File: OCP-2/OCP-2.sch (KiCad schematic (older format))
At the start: 176 parts, among them X1 ico*отверстие*М3, X2 ico*отверстие*М3, X3 ico*отверстие*М3, X4 ico*отверстие*М3

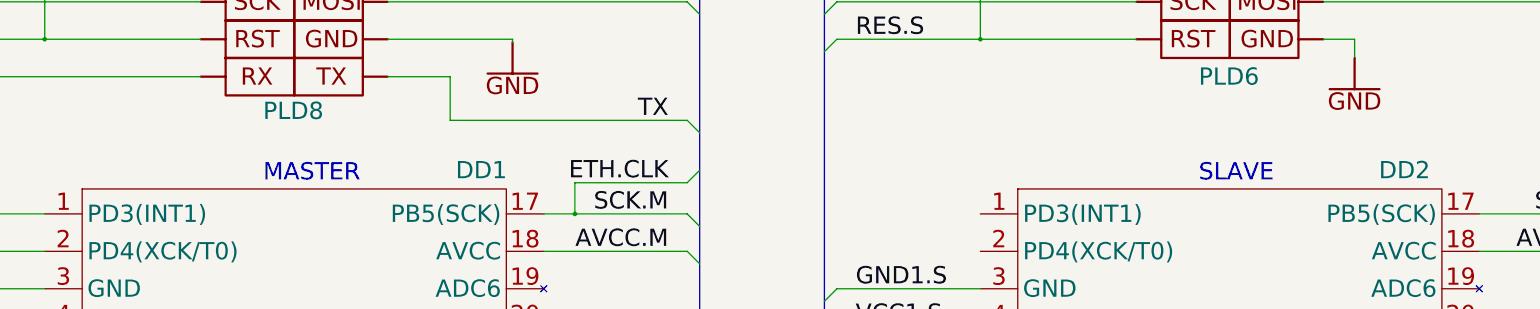
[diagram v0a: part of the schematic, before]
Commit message: перенесены клеммники, +LDO, +прог.разъем, +МК расположение
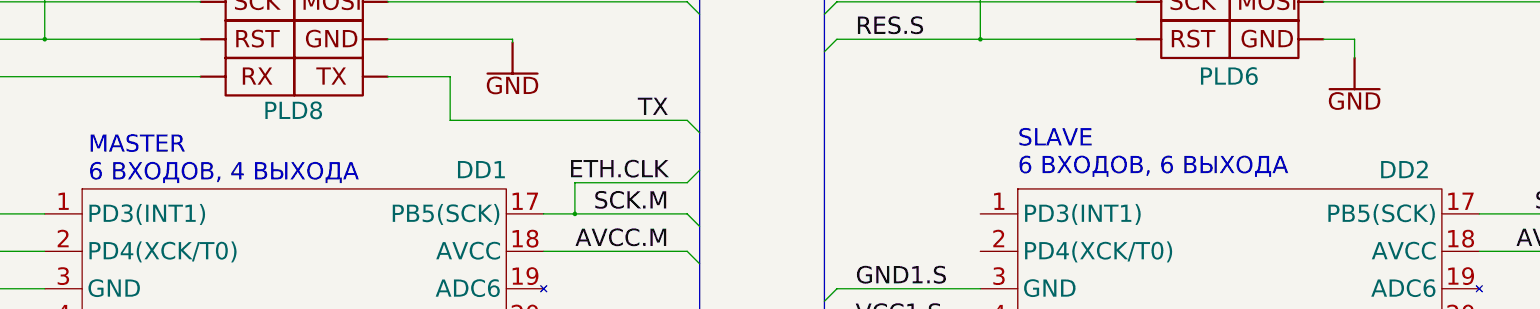
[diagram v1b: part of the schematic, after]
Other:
- note added: "MASTER\n6 ВХОДОВ, 4 ВЫХОДА"
- note added: "SLAVE\n6 ВХОДОВ, 6 ВЫХОДА"
- note removed: "MASTER"
- note removed: "SLAVE"
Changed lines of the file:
@@
 Wire Wire Line
 	21100 19250 23500 19250
-Text Notes 9000 9750 0    138  ~ 0
-MASTER
-Text Notes 16500 9750 0    138  ~ 0
-SLAVE
+Text Notes 7600 9750 0    138  ~ 0
+MASTER\n6 ВХОДОВ, 4 ВЫХОДА
+Text Notes 15050 9700 0    138  ~ 0
+SLAVE\n6 ВХОДОВ, 6 ВЫХОДА
 $Comp
 L eo-engine:Резистор*1кОм*0603 R65

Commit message: завершенеа трассировка
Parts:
- removed C11, C8: Конденсатор*10мкФ*16В*0805, N_RLC:Конденсатор_SMD_IEC_0805, symbol eo-engine:Конденсатор*10мкФ*16В*0805
- added C31: Конденсатор*10мкФ*16В*0805, N_RLC:Конденсатор_SMD_IEC_0805, symbol eo-engine:Конденсатор*10мкФ*16В*0805
- added X5: ico*LOGO_NIKITOS_10х10, N_ICO:ni_10x10, symbol eo-engine:ico*LOGO_NIKITOS_10х10
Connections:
- net 3V3: now also C31.1
- net DIN1: now also R46.2, XP16.4; no longer R43.2, XP16.1
- net DIN10: now also XP17.3; no longer XP18.2
- net DIN11: now also R51.2, XP17.2; no longer R53.2, XP18.3
- net DIN12: now also R50.2, XP17.1; no longer R54.2, XP18.4
- net DIN2: now also R47.2, XP16.3; no longer R44.2, XP16.2
- net DIN3: now also R48.2, XP16.2; no longer R45.2, XP16.3
- net DIN4: now also R49.2, XP16.1; no longer R46.2, XP16.4
- net DIN5: now also R45.2, XP18.4; no longer R47.2, XP17.1
- net DIN6: now also R44.2, XP18.3; no longer R48.2, XP17.2
- net DIN7: now also R43.2, XP18.2; no longer R49.2, XP17.3
- net DIN8: now also R54.2, XP18.1; no longer R50.2, XP17.4
- net DIN9: now also R53.2, XP17.4; no longer R51.2, XP18.1
- net GND: now also C31.2
- net MC.DIN1: now also C16.2, DD1.24 (PC1(ADC1)), R46.1, VD24.2; no longer C13.2, DD1.1 (PD3(INT1)), R43.1, VD21.2
- net MC.DIN10: now also DD2.31 (PD1(TXD)); no longer DD2.12 (PB0(ICP1))
- net MC.DIN11: now also C21.2, DD2.32 (PD2(INT0)), R51.1, VD29.2; no longer C23.2, DD2.13 (PB1(OC1A)), R53.1, VD31.2
- net MC.DIN12: now also C20.2, DD2.1 (PD3(INT1)), R50.1, VD28.2; no longer C24.2, DD2.14 (PB2(SS/OC1B)), R54.1, VD32.2
- net MC.DIN2: now also C17.2, DD1.23 (PCO(ADC0)), R47.1, VD25.2; no longer C14.2, DD1.2 (PD4(XCK/T0)), R44.1, VD22.2
- net MC.DIN3: now also C18.2, DD1.22 (ADC7), R48.1, VD26.2; no longer C15.2, DD1.9 (PD5(T1)), R45.1, VD23.2
- net MC.DIN4: now also C19.2, DD1.19 (ADC6), R49.1, VD27.2; no longer C16.2, DD1.10 (PD6(AIN0)), R46.1, VD24.2
- net MC.DIN5: now also C15.2, DD1.25 (PC2(ADC2)), R45.1, VD23.2; no longer C17.2, DD1.11 (PD7(AIN1)), R47.1, VD25.2
- net MC.DIN6: now also C14.2, DD1.26 (PC3(ADC3)), R44.1, VD22.2; no longer C18.2, DD1.12 (PB0(ICP1)), R48.1, VD26.2
- net MC.DIN7: now also C13.2, DD1.1 (PD3(INT1)), R43.1, VD21.2; no longer C19.2, DD2.9 (PD5(T1)), R49.1, VD27.2
- net MC.DIN8: now also C24.2, DD1.2 (PD4(XCK/T0)), R54.1, VD32.2; no longer C20.2, DD2.10 (PD6(AIN0)), R50.1, VD28.2
- net MC.DIN9: now also C23.2, DD2.30 (PD0(RXD)), R53.1, VD31.2; no longer C21.2, DD2.11 (PD7(AIN1)), R51.1, VD29.2
- net MC.OUT1: now also DD1.12 (PB0(ICP1)); no longer DD1.23 (PCO(ADC0))
- net MC.OUT10: now also DD2.11 (PD7(AIN1)); no longer DD2.31 (PD1(TXD))
- net MC.OUT2: now also DD1.11 (PD7(AIN1)); no longer DD1.24 (PC1(ADC1))
- net MC.OUT3: now also DD1.10 (PD6(AIN0)); no longer DD1.25 (PC2(ADC2))
- net MC.OUT4: now also DD1.9 (PD5(T1)); no longer DD1.26 (PC3(ADC3))
- net MC.OUT5: now also DD1.8 (PB7(XTAL2)); no longer DD2.23 (PCO(ADC0))
- net MC.OUT6: now also DD1.7 (PB6(XTAL1)); no longer DD2.24 (PC1(ADC1))
- net MC.OUT7: now also DD2.14 (PB2(SS/OC1B)); no longer DD2.25 (PC2(ADC2))
- net MC.OUT8: now also DD2.13 (PB1(OC1A)); no longer DD2.26 (PC3(ADC3))
- net MC.OUT9: now also DD2.12 (PB0(ICP1)); no longer DD2.30 (PD0(RXD))
- no-connect marks 16 -> 19
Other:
- note added: "MASTER\n8 ВХОДОВ, 6 ВЫХОДОВ"
- note added: "SLAVE\n4 ВХОДА, 4 ВЫХОДА"
- note removed: "MASTER\n6 ВХОДОВ, 4 ВЫХОДА"
- note removed: "SLAVE\n6 ВХОДОВ, 6 ВЫХОДА"
- moved on the sheet: C13, C14, C15, C16, C17, C18, C19, C20, C21, C22, C23, C24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

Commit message: добавлена поясняющая маркировка
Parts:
- renumbered C29 to C1, C1 to C10, C2 to C11, C3 to C12, C4 to C13, C5 to C14, C6 to C15, C27 to C16, C28 to C17, C20 to C18, C21 to C19, C30 to C2, C22 to C20, C23 to C21, C24 to C22, C13 to C23, C14 to C24, C15 to C25, C19 to C26, C18 to C27, C17 to C28, C16 to C29, C25 to C3, C7 to C4, C9 to C5, C26 to C6, C31 to C7, C10 to C8, C12 to C9, R60 to R1, R2 to R10, R64 to R11, R65 to R12, R59 to R13, R3 to R14, R4 to R15, R5 to R16, R6 to R17, R7 to R18, R8 to R19, R61 to R2, R9 to R20, R10 to R21, R11 to R22, R12 to R23, R13 to R24, R14 to R25, R15 to R26, R16 to R27, R17 to R28, R18 to R29, R55 to R3, R19 to R30, R20 to R31, R21 to R32, R22 to R33, R23 to R34, R24 to R35, R25 to R36, R26 to R37, R27 to R38, R28 to R39, R56 to R4, R29 to R40, R30 to R41, R31 to R42, R32 to R43, R33 to R44, R34 to R45, R35 to R46, R36 to R47, R37 to R48, R38 to R49, R57 to R5, R39 to R50, R40 to R51, R41 to R52, R42 to R53, R50 to R54, R51 to R55, R52 to R56, R53 to R57, R54 to R58, R43 to R59, R58 to R6, R44 to R60, R45 to R61, R49 to R62, R48 to R63, R47 to R64, R46 to R65, R1 to R7, R62 to R8, R63 to R9, VD28 to VD21, VD29 to VD22, VD30 to VD23, VD31 to VD24, VD32 to VD25, VD21 to VD26, VD22 to VD27, VD23 to VD28, VD27 to VD29, VD26 to VD30, VD25 to VD31, VD24 to VD32, XP2 to XP1, XP9 to XP10, XP10 to XP11, XP11 to XP12, XP12 to XP13, XP13 to XP14, XP17 to XP16, XP18 to XP17, XP16 to XP18, XP19 to XP2, XP1 to XP3, XP14 to XP9, XS2 to XS1
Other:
- note added: "вход мб 12В,\nкондей заменить на 25В"
- moved on the sheet: C18, C19, C20, C21, C22, C23, C24, C25, C26, C27, C28, C29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

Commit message: добавлены запирающие диоды в npn канал, обновлен step
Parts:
- added VD33, VD34, VD35, VD36, VD37, VD38, VD39, VD40, VD41, VD42: Диод*75В*0,2А*SOD-323, N_VD_HL:D_SOD-323_HandSoldering, symbol eo-engine:Диод*75В*0,2А*SOD-323
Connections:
- net DOUT1.NPN: now also VD33.1; no longer R29.1
- net DOUT10.NPN: now also VD42.1; no longer R53.1
- net DOUT2.NPN: now also VD34.1; no longer R30.1
- net DOUT3.NPN: now also VD35.1; no longer R31.1
- net DOUT4.NPN: now also VD36.1; no longer R32.1
- net DOUT5.NPN: now also VD37.1; no longer R33.1
- net DOUT6.NPN: now also VD38.1; no longer R49.1
- net DOUT7.NPN: now also VD39.1; no longer R50.1
- net DOUT8.NPN: now also VD40.1; no longer R51.1
- net DOUT9.NPN: now also VD41.1; no longer R52.1
- new net: R29.1, VD33.2
- new net: R30.1, VD34.2
- new net: R31.1, VD35.2
- new net: R32.1, VD36.2
- new net: R33.1, VD37.2
- new net: R49.1, VD38.2
- new net: R50.1, VD39.2
- new net: R51.1, VD40.2
- new net: R52.1, VD41.2
- new net: R53.1, VD42.2
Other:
- moved on the sheet: R14, R16, R18, R20, R22, R29, R30, R31, R32, R33, R34, R36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

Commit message: 0А: добавлены диодная защита прог. + стабилитрон на входе питания
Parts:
- added VD1, VD3: Диод*75В*0,2А*SOD-323, N_VD_HL:D_SOD-323_HandSoldering, symbol eo-engine:Диод*75В*0,2А*SOD-323
- added VD2: Стабилитрон*7,5В*SOD80, N_VD_HL:SOD-80, symbol eo-engine:Стабилитрон*15В*SOD80
- VD10: renamed from VD2; symbol eo-engine:Стабилитрон*7,5В*SOD80 -> eo-engine:Стабилитрон*15В*SOD80; COST 4 -> 0.92; INFO 7,5В -> 15В; LINK https://www.chipdip.ru/product/bzv55-c7v5.115 -> https://www.terraelectronica.ru/product/176228
- VD11: renamed from VD3; symbol eo-engine:Стабилитрон*7,5В*SOD80 -> eo-engine:Стабилитрон*15В*SOD80; COST 4 -> 0.92; INFO 7,5В -> 15В; LINK https://www.chipdip.ru/product/bzv55-c7v5.115 -> https://www.terraelectronica.ru/product/176228
- VD12: renamed from VD4; symbol eo-engine:Стабилитрон*7,5В*SOD80 -> eo-engine:Стабилитрон*15В*SOD80; COST 4 -> 0.92; INFO 7,5В -> 15В; LINK https://www.chipdip.ru/product/bzv55-c7v5.115 -> https://www.terraelectronica.ru/product/176228
- VD13: renamed from VD5; symbol eo-engine:Стабилитрон*7,5В*SOD80 -> eo-engine:Стабилитрон*15В*SOD80; COST 4 -> 0.92; INFO 7,5В -> 15В; LINK https://www.chipdip.ru/product/bzv55-c7v5.115 -> https://www.terraelectronica.ru/product/176228
- VD24: renamed from VD11; symbol eo-engine:Стабилитрон*7,5В*SOD80 -> eo-engine:Стабилитрон*15В*SOD80; COST 4 -> 0.92; INFO 7,5В -> 15В; LINK https://www.chipdip.ru/product/bzv55-c7v5.115 -> https://www.terraelectronica.ru/product/176228
- VD25: renamed from VD12; symbol eo-engine:Стабилитрон*7,5В*SOD80 -> eo-engine:Стабилитрон*15В*SOD80; COST 4 -> 0.92; INFO 7,5В -> 15В; LINK https://www.chipdip.ru/product/bzv55-c7v5.115 -> https://www.terraelectronica.ru/product/176228
- VD26: renamed from VD13; symbol eo-engine:Стабилитрон*7,5В*SOD80 -> eo-engine:Стабилитрон*15В*SOD80; COST 4 -> 0.92; INFO 7,5В -> 15В; LINK https://www.chipdip.ru/product/bzv55-c7v5.115 -> https://www.terraelectronica.ru/product/176228
- VD27: renamed from VD14; symbol eo-engine:Стабилитрон*7,5В*SOD80 -> eo-engine:Стабилитрон*15В*SOD80; COST 4 -> 0.92; INFO 7,5В -> 15В; LINK https://www.chipdip.ru/product/bzv55-c7v5.115 -> https://www.terraelectronica.ru/product/176228
- VD28: renamed from VD15; symbol eo-engine:Стабилитрон*7,5В*SOD80 -> eo-engine:Стабилитрон*15В*SOD80; COST 4 -> 0.92; INFO 7,5В -> 15В; LINK https://www.chipdip.ru/product/bzv55-c7v5.115 -> https://www.terraelectronica.ru/product/176228
- VD9: renamed from VD1; symbol eo-engine:Стабилитрон*7,5В*SOD80 -> eo-engine:Стабилитрон*15В*SOD80; COST 4 -> 0.92; INFO 7,5В -> 15В; LINK https://www.chipdip.ru/product/bzv55-c7v5.115 -> https://www.terraelectronica.ru/product/176228
- renumbered C4 to C3, C5 to C4, C3 to C5, R16 to R15, R18 to R16, R20 to R17, R22 to R18, R15 to R19, R17 to R20, R19 to R21, R21 to R22, R36 to R35, R38 to R36, R40 to R37, R42 to R38, R35 to R39, R37 to R40, R39 to R41, R41 to R42, VD6 to VD14, VD7 to VD15, VD8 to VD16, VD9 to VD17, VD10 to VD18, VD38 to VD19, VD39 to VD20, VD40 to VD21, VD41 to VD22, VD42 to VD23, VD16 to VD29, VD17 to VD30, VD18 to VD31, VD19 to VD32, VD20 to VD33, VD21 to VD34, VD22 to VD35, VD23 to VD36, VD24 to VD37, VD25 to VD38, VD26 to VD39, VD33 to VD4, VD27 to VD40, VD28 to VD41, VD29 to VD42, VD30 to VD43, VD31 to VD44, VD32 to VD45, VD34 to VD5, VD35 to VD6, VD36 to VD7, VD37 to VD8
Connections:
- net GND: now also VD2.1
- net 5V renamed 4...15V
- net 4...15V: now also VD1.1, VD2.2, VD3.1; no longer XP1.1B, XP3.1B
- new net 5V.M: VD1.2, XP1.1B
- new net 5V.S: VD3.2, XP3.1B
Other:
- moved on the sheet: C5, C6, C7, G1, XP2

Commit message: ссылки в элементах исправлены под заказ
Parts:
- C1, C11, C12, C13, C14, C15, C18, C19, C2, C20, C21, C22, C23, C24, C25, C26, C27, C28, C29, C4, C9: COST (none) -> 0.26
- C10, C3, C5, C6, C7, C8: COST (none) -> 0.89
- C16, C17: COST (none) -> 0.22
- DD1: COST 205 -> 390; INFO ATmega168 -> ATmega328; LINK https://www.terraelectronica.ru/product/1907917 -> https://www.chipdip.ru/product/atmega168v-10au
- DD2: COST 130 -> 137; INFO ATmega88 -> ATmega48; LINK https://www.terraelectronica.ru/product/1908354 -> https://www.terraelectronica.ru/product/1908181
- DD3: COST 350 -> 352
- G1: COST (none) -> 15
- R1, R11, R12, R19, R2, R20, R21, R22, R23, R29, R30, R31, R32, R33, R39, R40, R41, R42, R43, R49, R50, R51, R52, R53, R54, R55, R56, R57, R58, R59, R60, R61, R62, R63, R64, R65: COST (none) -> 0,14; LINK (none) -> https://www.terraelectronica.ru/product/2128053
- R10, R14, R15, R16, R17, R18, R24, R25, R26, R27, R28, R34, R35, R36, R37, R38, R44, R45, R46, R47, R48, R7, R8, R9: COST (none) -> 0,17; LINK (none) -> https://www.terraelectronica.ru/product/2127758
- R13: COST (none) -> 2,8; LINK (none) -> https://www.terraelectronica.ru/product/819708
- R3, R4, R5, R6: COST 0,16 -> 0.16
- VD1, VD19, VD20, VD21, VD22, VD23, VD3, VD4, VD5, VD6, VD7, VD8: COST 13 -> 3,3; LINK https://www.chipdip.ru/product/bas416.115 -> https://www.terraelectronica.ru/product/242660
- VD10, VD11, VD12, VD13, VD2, VD24, VD25, VD26, VD27, VD28, VD9: value Стабилитрон*7,5В*SOD80 -> Стабилитрон*15В*SOD80
- VD14, VD15, VD16, VD17, VD18, VD29, VD30, VD31, VD32, VD33: value Стабилитрон*7,5В*SOD80 -> Стабилитрон*15В*SOD80; symbol eo-engine:Стабилитрон*7,5В*SOD80 -> eo-engine:Стабилитрон*15В*SOD80; COST 4 -> 0.92; INFO 7,5В -> 15В; LINK https://www.chipdip.ru/product/bzv55-c7v5.115 -> https://www.terraelectronica.ru/product/176228
- VD34, VD35, VD36, VD37, VD38, VD39, VD40, VD41, VD42, VD43, VD44, VD45: COST 1,3 -> 1.4
- X1, X2, X3, X4: COST (none) -> 0; INFO (none) -> PCB_element; LINK (none) -> -
- X5: COST (none) -> 0; LINK (none) -> -
- XP1, XP3: COST (none) -> 8
- XP10, XP11, XP12, XP13, XP14, XP4, XP5, XP6, XP7, XP8: COST (none) -> 6.3; LINK (none) -> https://www.terraelectronica.ru/product/878568
- XP15, XP16, XP17, XP18, XP9: COST (none) -> 11.9
- XP2: COST (none) -> 7.4
- XS1: COST (none) -> 250
- ZQ1: COST (none) -> 21.9

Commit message: перечень ПКИ для КД
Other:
- note removed: "подключить SPI"
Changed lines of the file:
@@
 Entry Wire Line
 	21000 11950 21100 12050
-Text Notes 21450 8125 0    138  ~ 0
-подключить SPI
 NoConn ~ 3250 4300
 Text Label 28000 9050 2    138  ~ 0
@@
 Wire Wire Line
 	52150 10400 52150 17800
-Text Notes 9500 2000 0    138  ~ 0
-вход мб 12В,\nкондей заменить на 25В
 $Comp
 L eo-engine:Диод*75В*0,2А*SOD-323 VD4
@@
 Wire Bus Line
 	12500 8000 12500 20000
+Text Notes 9500 2000 0    138  ~ 0
+вход мб 12В,\nкондей заменить на 25В
 $EndSCHEMATC
